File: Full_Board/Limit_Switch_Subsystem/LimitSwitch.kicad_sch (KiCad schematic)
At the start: 7 parts, among them J20 OQ0212500000G, U17 UCLAMP3301H.TCT

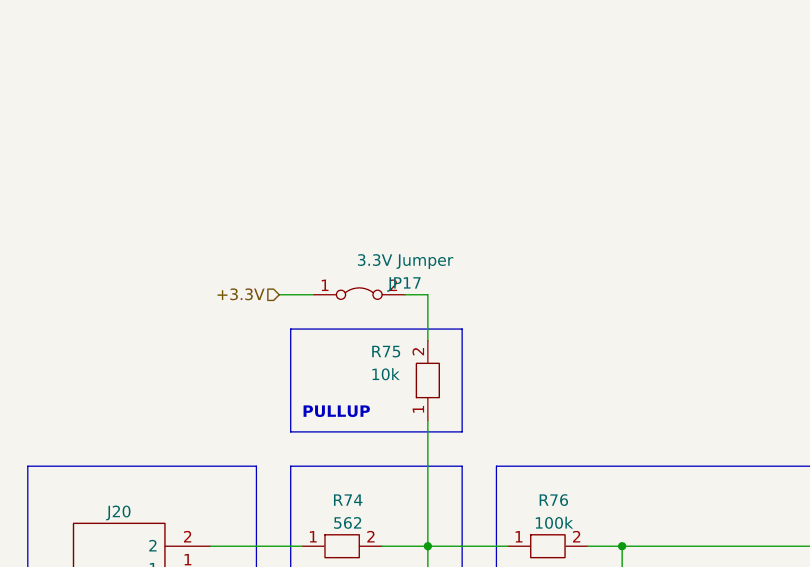
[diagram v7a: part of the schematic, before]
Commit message: Cleanup all schematics and project libs
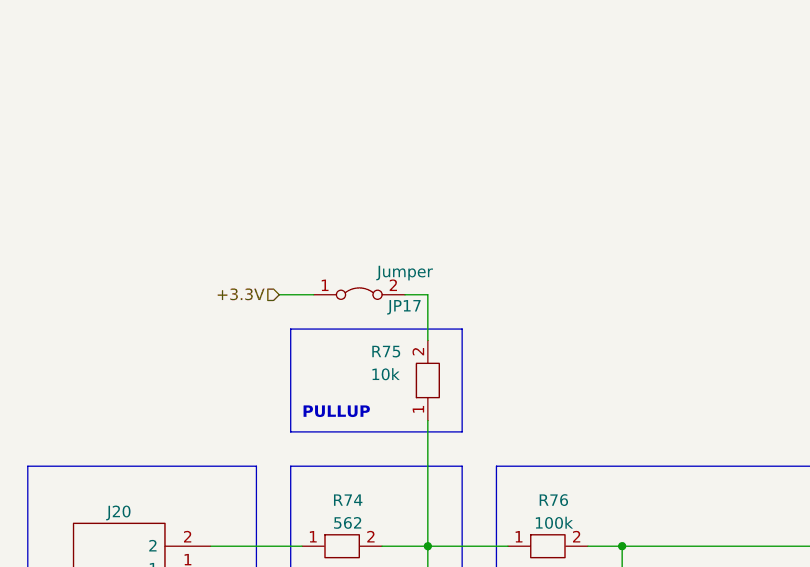
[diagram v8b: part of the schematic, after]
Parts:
- C37: Digikey Link (none) -> https://www.digikey.com/en/products/detail/kemet/C1210C822K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; Digikey link https://www.digikey.com/en/products/detail/kemet/C1210C822K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 -> (none); Mouser Link (none) -> https://www.mouser.com/ProductDetail/KEMET/C1210C822K2RACAU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; Mouser link https://www.mouser.com/ProductDetail/KEMET/C1210C822K2RACAU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 -> (none)
- J20: Digikey link https://www.digikey.com/en/products/detail/amphenol-anytek/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 -> (none); Height 9.2 -> (none); Manufacturer_Name Amphenol -> (none); Manufacturer_Part_Number OQ0212500000G -> (none); Mouser Link (none) -> https://www.mouser.com/ProductDetail/Amphenol-Anytek/OQ0212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; Mouser Price/Stock https://www.mouser.co.uk/ProductDetail/Amphenol-Anytek/OQ02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 -> (none); Mouser link https://www.mouser.com/ProductDetail/Amphenol-Anytek/OQ0212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 -> (none)
- JP17: value 3.3V Jumper -> Jumper; symbol Jumper:Jumper_2_Bridged -> PH1-02-UA:PH1-02-UA; Digikey Link https://www.digikey.com/en/products/detail/adam-tech/PH1-02-UA/9830266 -> https://www.digikey.com/en/products/detail/adam-tech/PH1-02-UA/9830266?s=N4IgTCBcDa4AwFYDsBaACgCQIwrmFAqgIIoByAIiALoC%2BQA; Manufacturer's Part Number (none) -> PH1-02-UA; Manufacturers Part Number PH1-02-UA -> (none)
- R74: Digikey Link (none) -> https://www.digikey.com/en/products/detail/bourns-inc/CR040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; Digikey link https://www.digikey.com/en/products/detail/bourns-inc/CR040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 -> (none); Mouse link https://www.mouser.com/ProductDetail/Bourns/CR0402-FX-5620G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 -> (none); Mouser Link (none) -> https://www.mouser.com/ProductDetail/Bourns/CR0402-FX-5620G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; Mouser link https://www.mouser.com/ProductDetail/Bourns/CR0402-FX-5620G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 -> (none)
- R75: Digikey Link (none) -> https://www.digikey.com/en/products/detail/stackpole-electr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; Digikey link https://www.digikey.com/en/products/detail/stackpole-electr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 -> (none)
- R76: Digikey Link (none) -> https://www.digikey.com/en/products/detail/vishay-dale/RCV2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; Digikey link https://www.digikey.com/en/products/detail/vishay-dale/RCV2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 -> (none); Mouser Link (none) -> https://www.mouser.com/ProductDetail/Vishay-Draloric/RCV251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; Mouser link https://www.mouser.com/ProductDetail/Vishay-Draloric/RCV251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 -> (none)
- U17: Manufacturer's Part Number (none) -> UCLAMP3301H.TCT; Manufacturers Part Number UCLAMP3301H.TCT -> (none); Mouser Link (none) -> https://www.mouser.com/ProductDetail/Semtech/UCLAMP3301H.TC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; Mouser Part Number (none) -> 947-UCLAMP3301H.TCT
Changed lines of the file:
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@@
-      (effects (font (size 1.27 1.27)) (justify left) hide)
-    )
-    (property "Manufacturer_Part_Number" "OQ0212500000G" (id 4) (at 102.87 77.47 0)
       (effects (font (size 1.27 1.27)) (justify left) hide)
     )
@@
       (effects (font (size 1.27 1.27)) hide)
     )
-    (property "Mouser Link" "" (id 8) (at 119.38 92.71 0)
-      (effects (font (size 1.27 1.27)) hide)
-    )
-    (property "Description" "Pluggable Terminal Blocks 2P 3.50MM HDR STR PLUGGABLE TERM BLK" (id 9) (at 102.87 90.17 0)
-      (effects (font (size 1.27 1.27)) (justify left) hide)
-    )
-    (property "Height" "9.2" (id 10) (at 102.87 87.63 0)
-      (effects (font (size 1.27 1.27)) (justify left) hide)
-    )
-    (property "Mouser Price/Stock" "https://www.mouser.co.uk/ProductDetail/Amphenol-Anytek/OQ0212500000G?qs=Mv7BduZupUhn3%2FKe8nJdbQ%3D%3D" (id 11) (at 102.87 82.55 0)
-      (effects (font (size 1.27 1.27)) (justify left) hide)
-    )
-    (property "Manufacturer_Name" "Amphenol" (id 12) (at 102.87 80.01 0)
-      (effects (font (size 1.27 1.27)) (justify left) hide)
-    )
-    (property "Digikey link" "https://www.digikey.com/en/products/detail/amphenol-anytek/OQ0212500000G/4242016" (id 13) (at 119.38 92.71 0)
+    (property "Mouser Link" "https://www.mouser.com/ProductDetail/Amphenol-Anytek/OQ0212500000G?qs=Mv7BduZupUhn3/Ke8nJdbQ%3D%3D" (id 8) (at 119.38 92.71 0)
       (effects (font (size 1.27 1.27)) hide)
     )
     (property "Manufacturer's Part Number" "OQ0212500000G" (id 14) (at 119.38 92.71 0)
-      (effects (font (size 1.27 1.27)) hide)
-    )
-    (property "Mouser link" "https://www.mouser.com/ProductDetail/Amphenol-Anytek/OQ0212500000G?qs=Mv7BduZupUhn3%2FKe8nJdbQ%3D%3D" (id 15) (at 119.38 92.71 0)
       (effects (font (size 1.27 1.27)) hide)
     )
@@
       (effects (font (size 1.27 1.27)) (justify left) hide)
     )
-    (property "Digikey link" "https://www.digikey.com/en/products/detail/bourns-inc/CR0402-FX-5620GLF/3783429?s=N4IgTCBcDaIAQGEBKAGALCsBaAYgDSwFYA2MFAcQBkcQBdAXyA" (id 7) (at 143.51 101.6 0)
+    (property "Digikey Link" "https://www.digikey.com/en/products/detail/bourns-inc/CR0402-FX-5620GLF/3783429?s=N4IgTCBcDaIAQGEBKAGALCsBaAYgDSwFYA2MFAcQBkcQBdAXyA" (id 7) (at 143.51 101.6 0)
       (effects (font (size 1.27 1.27)) (justify left) hide)
     )
-    (property "Mouse link" "https://www.mouser.com/ProductDetail/Bourns/CR0402-FX-5620GLF?qs=sGAEpiMZZMtlubZbdhIBIDfFWzqdPB9%252B4rUQL12%252Bb9s%3D" (id 8) (at 143.51 104.14 0)
+    (property "Mouser Link" "https://www.mouser.com/ProductDetail/Bourns/CR0402-FX-5620GLF?qs=sGAEpiMZZMtlubZbdhIBIDfFWzqdPB9%252B4rUQL12%252Bb9s%3D" (id 8) (at 143.51 104.14 0)
       (effects (font (size 1.27 1.27)) (justify left) hide)
-    )
-    (property "Mouser link" "https://www.mouser.com/ProductDetail/Bourns/CR0402-FX-5620GLF?qs=sGAEpiMZZMtlubZbdhIBIDfFWzqdPB9%252B4rUQL12%252Bb9s%3D" (id 9) (at 129.54 90.17 0)
-      (effects (font (size 1.27 1.27)) hide)
     )
     (pin "1")
@@
       (effects (font (size 1.27 1.27)) (justify left) hide)
     )
-    (property "Digikey link" "https://www.digikey.com/en/products/detail/stackpole-electronics-inc/RMCF1206FT10K0/1759669" (id 7) (at 154.94 62.23 0)
+    (property "Digikey Link" "https://www.digikey.com/en/products/detail/stackpole-electronics-inc/RMCF1206FT10K0/1759669" (id 7) (at 154.94 62.23 0)
       (effects (font (size 1.27 1.27)) (justify left) hide)
     )
-    (property "Mouser link" "" (id 8) (at 157.48 62.23 0)
+    (property "Mouser Link" "" (id 8) (at 157.48 62.23 0)
       (effects (font (size 1.27 1.27)) (justify left) hide)
     )
@@
       (effects (font (size 1.27 1.27)) (justify left) hide)
     )
-    (property "Digikey link" "https://www.digikey.com/en/products/detail/vishay-dale/RCV2512100KFKEGAT/13985179?s=N4IgTCBcDaIEoGEBqYCsBGM6AM2DSAYngKIDiAggCoAEIAugL5A" (id 7) (at 166.37 104.14 0)
+    (property "Digikey Link" "https://www.digikey.com/en/products/detail/vishay-dale/RCV2512100KFKEGAT/13985179?s=N4IgTCBcDaIEoGEBqYCsBGM6AM2DSAYngKIDiAggCoAEIAugL5A" (id 7) (at 166.37 104.14 0)
       (effects (font (size 1.27 1.27)) (justify left) hide)
     )
-    (property "Mouser link" "https://www.mouser.com/ProductDetail/Vishay-Draloric/RCV2512100KFKEGAT?qs=sGAEpiMZZMtlubZbdhIBIOK8YY79HZuiqCZ6uF64pjM%3D" (id 8) (at 166.37 101.6 0)
+    (property "Mouser Link" "https://www.mouser.com/ProductDetail/Vishay-Draloric/RCV2512100KFKEGAT?qs=sGAEpiMZZMtlubZbdhIBIOK8YY79HZuiqCZ6uF64pjM%3D" (id 8) (at 166.37 101.6 0)
       (effects (font (size 1.27 1.27)) (justify left) hide)
     )
@@
       (effects (font (size 1.27 1.27)) (justify left) hide)
     )
-    (property "Digikey link" "https://www.digikey.com/en/products/detail/kemet/C1210C822K2RACAUTO/16524786?s=N4IgTCBcDaIMIEYwIAxwBxjAaTAJQEE4CBVAFQHkACEAXQF8g" (id 7) (at 154.94 92.71 0)
+    (property "Digikey Link" "https://www.digikey.com/en/products/detail/kemet/C1210C822K2RACAUTO/16524786?s=N4IgTCBcDaIMIEYwIAxwBxjAaTAJQEE4CBVAFQHkACEAXQF8g" (id 7) (at 154.94 92.71 0)
       (effects (font (size 1.27 1.27)) (justify left) hide)
     )
-    (property "Mouser link" "https://www.mouser.com/ProductDetail/KEMET/C1210C822K2RACAUTO?qs=sGAEpiMZZMukHu%252BjC5l7YfRfrXj%2FJXIdfvr9FKYreLc%3D" (id 8) (at 157.48 92.71 0)
+    (property "Mouser Link" "https://www.mouser.com/ProductDetail/KEMET/C1210C822K2RACAUTO?qs=sGAEpiMZZMukHu%252BjC5l7YfRfrXj%2FJXIdfvr9FKYreLc%3D" (id 8) (at 157.48 92.71 0)
       (effects (font (size 1.27 1.27)) (justify left) hide)
     )
@@
     (pin "2")
   )
-  (symbol (lib_id "Jumper:Jumper_2_Bridged") (at 135.89 62.23 0) (unit 1)
+  (symbol (lib_id "PH1-02-UA:PH1-02-UA") (at 135.89 64.77 0) (unit 1)
     (in_bom yes) (on_board yes)
-    (property "Reference" "JP17" (id 0) (at 140.97 60.96 0))
-    (property "Value" "3.3V Jumper" (id 1) (at 140.97 58.42 0))
-    (property "Footprint" "TestPoint:TestPoint_2Pads_Pitch2.54mm_Drill0.8mm" (id 2) (at 135.89 62.23 0)
+    (property "Reference" "JP17" (id 0) (at 140.97 63.5 0))
+    (property "Value" "Jumper" (id 1) (at 140.97 59.69 0))
+    (property "Footprint" "TestPoint:TestPoint_2Pads_Pitch2.54mm_Drill0.8mm" (id 2) (at 135.89 64.77 0)
       (effects (font (size 1.27 1.27)) hide)
     )
-    (property "Datasheet" "~" (id 3) (at 135.89 62.23 0)
+    (property "Datasheet" "https://app.adam-tech.com/products/download/data_sheet/201605/ph1-xx-ua-data-sheet.pdf" (id 3) (at 135.89 64.77 0)
       (effects (font (size 1.27 1.27)) hide)
     )
-    (property "Manufacturers Part Number" "PH1-02-UA" (id 4) (at 135.89 62.23 0)
+    (property "Digikey Part Number" "2057-PH1-02-UA-ND" (id 5) (at 135.89 64.77 0)
       (effects (font (size 1.27 1.27)) hide)
     )
-    (property "Digikey Part Number" "2057-PH1-02-UA-ND" (id 5) (at 135.89 62.23 0)
+    (property "Mouser Part Number" "" (id 6) (at 135.89 64.77 0)
       (effects (font (size 1.27 1.27)) hide)
     )
-    (property "Mouser Part Number" "" (id 6) (at 135.89 62.23 0)
+    (property "Digikey Link" "https://www.digikey.com/en/products/detail/adam-tech/PH1-02-UA/9830266?s=N4IgTCBcDa4AwFYDsBaACgCQIwrmFAqgIIoByAIiALoC%2BQA" (id 7) (at 135.89 64.77 0)
       (effects (font (size 1.27 1.27)) hide)
     )
-    (property "Digikey Link" "https://www.digikey.com/en/products/detail/adam-tech/PH1-02-UA/9830266" (id 7) (at 135.89 62.23 0)
+    (property "Mouser Link" "" (id 8) (at 135.89 64.77 0)
       (effects (font (size 1.27 1.27)) hide)
     )
-    (property "Mouser Link" "" (id 8) (at 135.89 62.23 0)
+    (property "Manufacturer's Part Number" "PH1-02-UA" (id 9) (at 135.89 64.77 0)
       (effects (font (size 1.27 1.27)) hide)
     )
@@
       (effects (font (size 1.524 1.524)) hide)
     )
-    (property "Manufacturers Part Number" "UCLAMP3301H.TCT" (id 4) (at 151.13 123.19 0)
-      (effects (font (size 1.27 1.27)) hide)
-    )
     (property "Digikey Part Number" "UCLAMP3301HDKR-ND" (id 5) (at 153.67 124.46 0)
       (effects (font (size 1.27 1.27)) hide)
     )
-    (property "Mouser Part Number" "" (id 6) (at 165.1 127 0)
+    (property "Mouser Part Number" " 947-UCLAMP3301H.TCT " (id 6) (at 165.1 127 0)
       (effects (font (size 1.27 1.27)) hide)
     )
@@
       (effects (font (size 1.27 1.27)) hide)
     )
-    (property "Mouser Link" "" (id 8) (at 165.1 127 0)
+    (property "Mouser Link" "https://www.mouser.com/ProductDetail/Semtech/UCLAMP3301H.TCT?qs=rBWM4%252BvDhIeimYmappCp5Q%3D%3D" (id 8) (at 165.1 127 0)
       (effects (font (size 1.27 1.27)) hide)
     )
+    (property "Manufacturer's Part Number" "UCLAMP3301H.TCT" (id 9) (at 165.1 127 0)
+      (effects (font (size 1.27 1.27)) hide)
+    )
